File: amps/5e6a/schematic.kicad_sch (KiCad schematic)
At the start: 62 parts, among them T3 part not legible

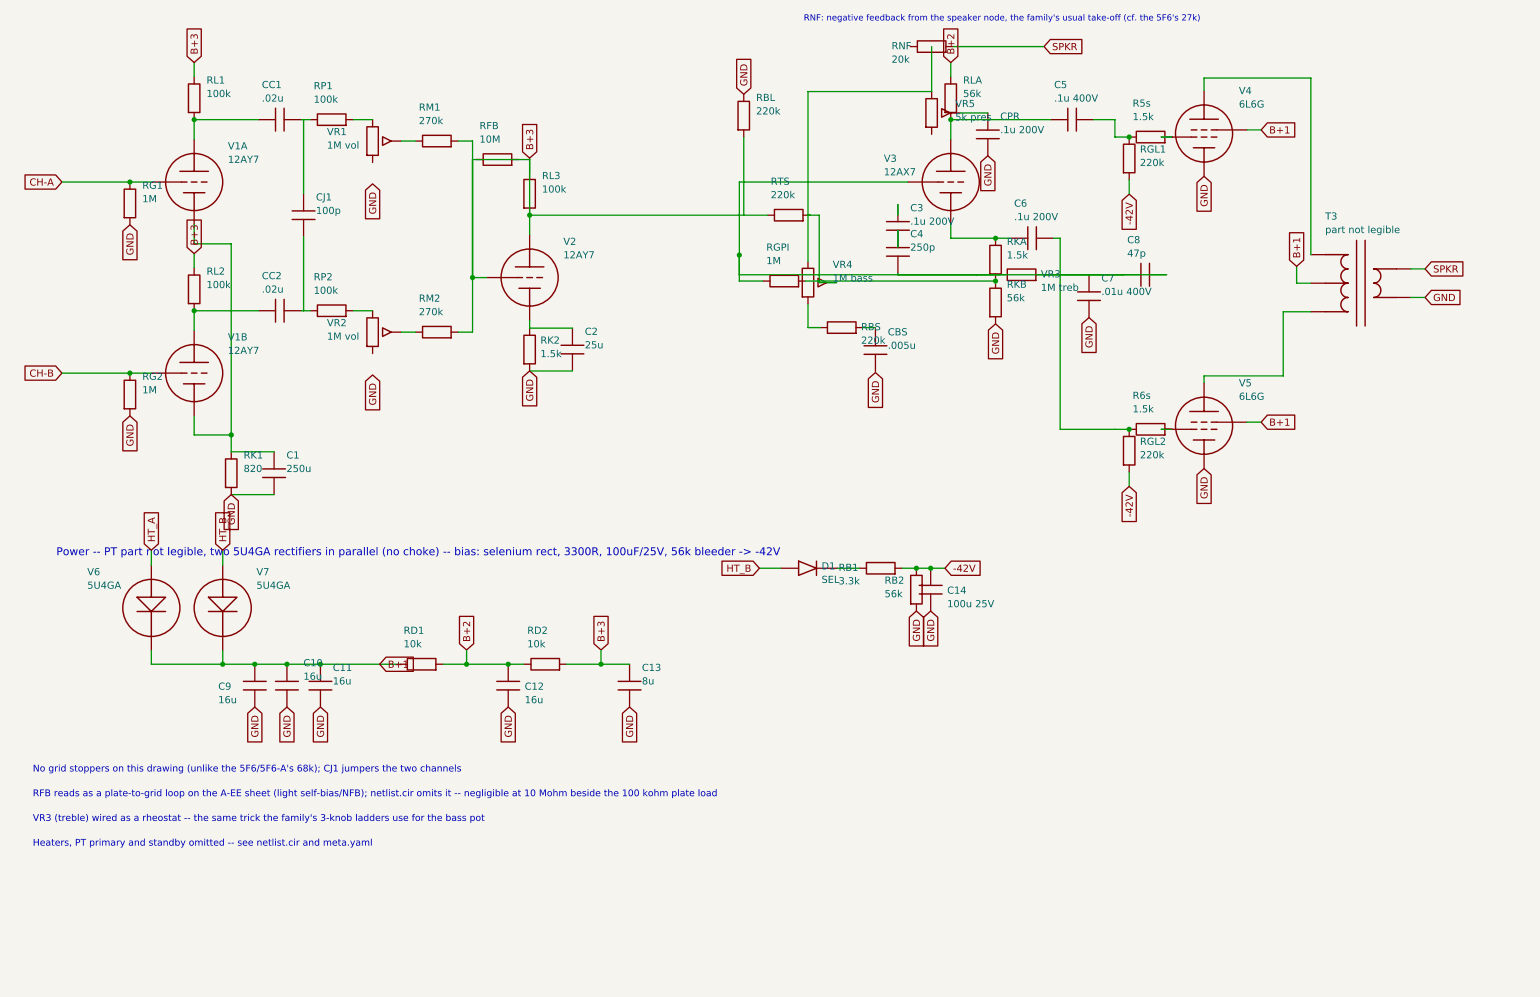
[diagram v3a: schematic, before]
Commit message: Fix: deterministic schematic ids and wires split at every join
- _u() is uuid5 over (amp id, emission order), so a regeneration of an
  unchanged script is byte-identical and a drift gate becomes possible
- write() splits wire segments at symbol pins, wire ends and junction dots,
  so the file connects exactly what the drawing shows under KiCad's
  endpoint-only semantics (270 pins were on a wire's interior; net
  partitions unchanged on all 38 sheets)
- all sheets regenerated; aa864-bassman title block was stale (draft) and
  now matches meta.yaml (verified)

Co-Authored-By: Claude Fable 5.1 <noreply@anthropic.com>
Claude-Session: https://claude.ai/code/session_01KBMfdh37HmCL2iWcBiL5J1
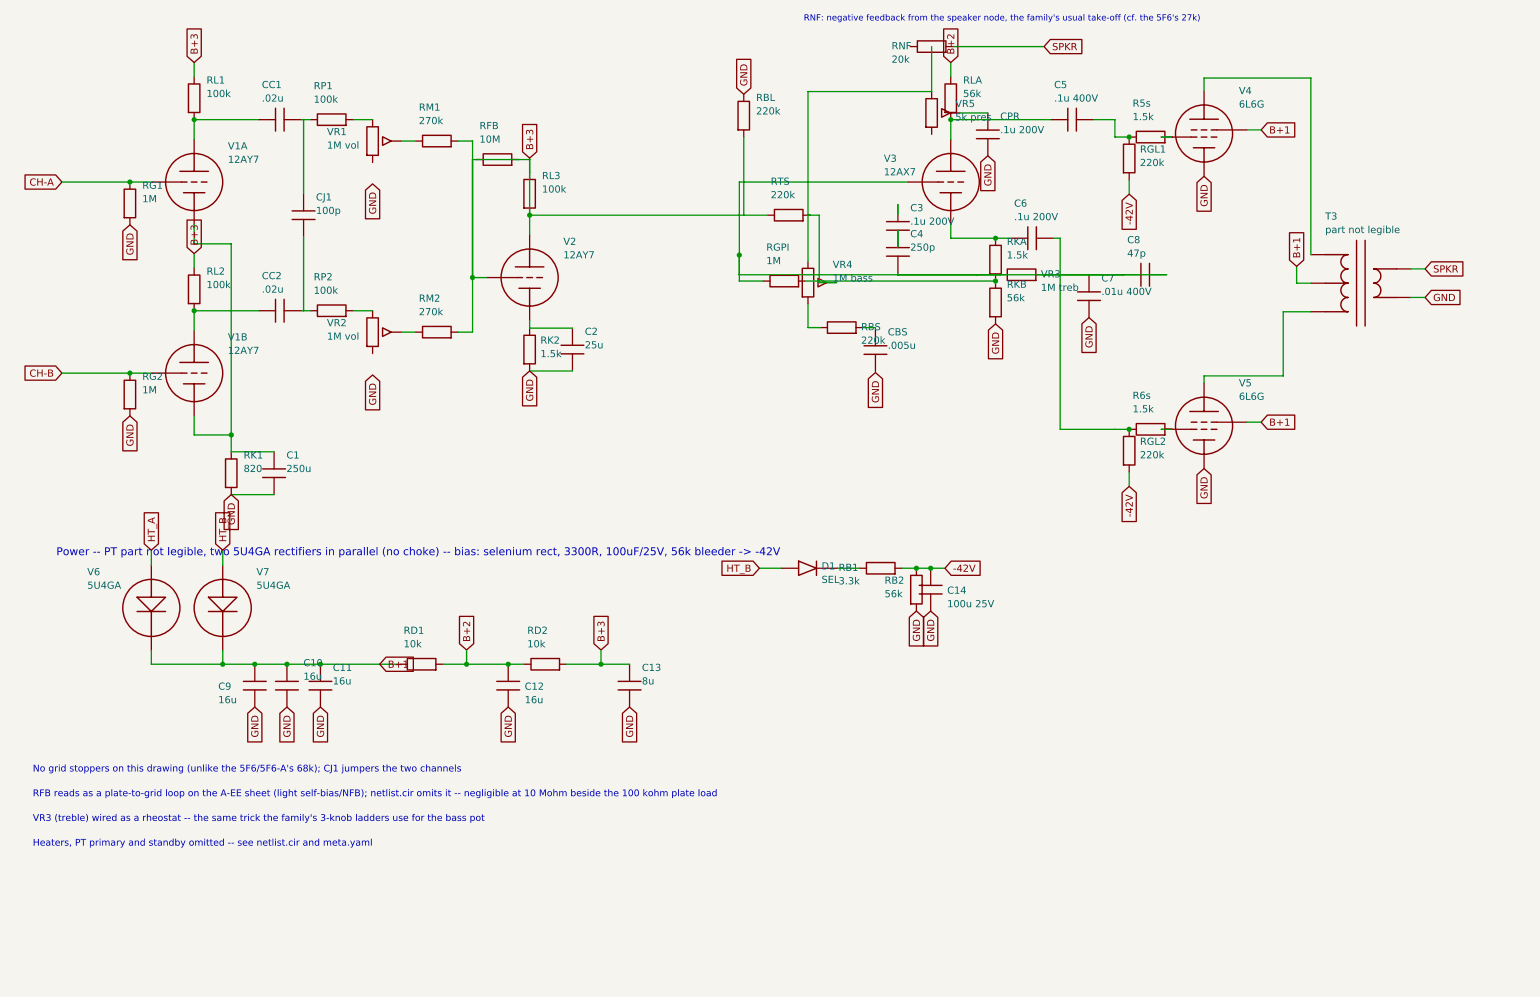
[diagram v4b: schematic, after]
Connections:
- net B+3: now also RFB.1, RFB.2
- net at RTS.2, VR4.2 (W): now also VR4.1, VR5.1
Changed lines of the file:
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@@
     (property "Reference" "V1A" (at 47.4116 36.07 0) (effects (font (size 1.27 1.27)) (justify left)))
     (property "Value" "12AY7" (at 47.4116 38.47 0) (effects (font (size 1.27 1.27)) (justify left))))
-  (wire (pts (xy 17.8816 42.47) (xy 33.7916 42.47))
+  (wire (pts (xy 17.8816 42.47) (xy 29.9816 42.47))
+    (stroke (width 0) (type default)))
+  (wire (pts (xy 29.9816 42.47) (xy 33.7916 42.47))
     (stroke (width 0) (type default)))
   (junction (at 29.9816 42.47) (diameter 0) (color 0 0 0 0))
@@
   (wire (pts (xy 88.4016 35.18) (xy 90.9416 35.18))
     (stroke (width 0) (type default)))
-  (wire (pts (xy 90.9416 35.18) (xy 90.9416 59.47))
+  (wire (pts (xy 90.9416 35.18) (xy 90.9416 38.47))
+    (stroke (width 0) (type default)))
+  (wire (pts (xy 90.9416 38.47) (xy 90.9416 59.47))
     (stroke (width 0) (type default)))
   (global_label "CH-B" (shape input) (at 17.8816 76.47 180)
@@
     (property "Reference" "V1B" (at 47.4116 70.07 0) (effects (font (size 1.27 1.27)) (justify left)))
     (property "Value" "12AY7" (at 47.4116 72.47 0) (effects (font (size 1.27 1.27)) (justify left))))
-  (wire (pts (xy 17.8816 76.47) (xy 33.7916 76.47))
+  (wire (pts (xy 17.8816 76.47) (xy 29.9816 76.47))
+    (stroke (width 0) (type default)))
+  (wire (pts (xy 29.9816 76.47) (xy 33.7916 76.47))
     (stroke (width 0) (type default)))
   (junction (at 29.9816 76.47) (diameter 0) (color 0 0 0 0))
@@
   (wire (pts (xy 41.4116 87.47) (xy 48.0116 87.47))
     (stroke (width 0) (type default)))
-  (wire (pts (xy 48.0116 53.47) (xy 48.0116 90.47))
+  (wire (pts (xy 48.0116 53.47) (xy 48.0116 87.47))
+    (stroke (width 0) (type default)))
+  (wire (pts (xy 48.0116 87.47) (xy 48.0116 90.47))
     (stroke (width 0) (type default)))
   (junction (at 48.0116 87.47) (diameter 0) (color 0 0 0 0))
@@
     (property "Reference" "RL3" (at 103.302 41.36 0) (effects (font (size 1.27 1.27)) (justify left)))
     (property "Value" "100k" (at 103.302 43.76 0) (effects (font (size 1.27 1.27)) (justify left))))
-  (wire (pts (xy 101.102 40.75) (xy 101.102 38.21))
+  (wire (pts (xy 101.102 40.75) (xy 101.102 38.47))
+    (stroke (width 0) (type default)))
+  (wire (pts (xy 101.102 38.47) (xy 101.102 38.21))
     (stroke (width 0) (type default)))
   (global_label "B+3" (shape input) (at 101.102 38.21 90)
     (effects (font (size 1.27 1.27)) (justify left)))
-  (wire (pts (xy 101.102 48.37) (xy 101.102 38.47))
-    (stroke (width 0) (type default)))
-  (wire (pts (xy 101.102 38.47) (xy 90.9416 38.47))
+  (wire (pts (xy 101.102 48.37) (xy 101.102 40.75))
+    (stroke (width 0) (type default)))
+  (wire (pts (xy 101.102 40.75) (xy 101.102 38.47))
+    (stroke (width 0) (type default)))
+  (wire (pts (xy 101.102 38.47) (xy 99.1916 38.47))
+    (stroke (width 0) (type default)))
+  (wire (pts (xy 99.1916 38.47) (xy 91.5716 38.47))
+    (stroke (width 0) (type default)))
+  (wire (pts (xy 91.5716 38.47) (xy 90.9416 38.47))
     (stroke (width 0) (type default)))
   (wire (pts (xy 90.9416 38.47) (xy 90.9416 59.47))
@@
     (property "Reference" "VR4" (at 155.032 57.17 0) (effects (font (size 1.27 1.27)) (justify left)))
     (property "Value" "1M bass" (at 155.032 59.57 0) (effects (font (size 1.27 1.27)) (justify left))))
-  (wire (pts (xy 150.632 48.37) (xy 152.632 48.37))
+  (wire (pts (xy 150.632 48.37) (xy 151.012 48.37))
+    (stroke (width 0) (type default)))
+  (wire (pts (xy 151.012 48.37) (xy 152.632 48.37))
     (stroke (width 0) (type default)))
   (wire (pts (xy 152.632 48.37) (xy 152.632 60.37))
@@
   (wire (pts (xy 152.632 60.37) (xy 155.712 60.37))
     (stroke (width 0) (type default)))
-  (wire (pts (xy 150.632 56.56) (xy 150.632 26.37))
+  (wire (pts (xy 150.632 56.56) (xy 150.632 48.37))
+    (stroke (width 0) (type default)))
+  (wire (pts (xy 150.632 48.37) (xy 150.632 26.37))
     (stroke (width 0) (type default)))
   (symbol (lib_id "cx:R") (at 156.632 68.37 90) (unit 1)
@@
     (property "Reference" "V3" (at 164.127 38.29 0) (effects (font (size 1.27 1.27)) (justify left)))
     (property "Value" "12AX7" (at 164.127 40.69 0) (effects (font (size 1.27 1.27)) (justify left))))
-  (wire (pts (xy 214.442 58.97) (xy 138.412 58.97))
-    (stroke (width 0) (type default)))
-  (wire (pts (xy 138.412 58.97) (xy 138.412 42.47))
+  (wire (pts (xy 214.442 58.97) (xy 206.822 58.97))
+    (stroke (width 0) (type default)))
+  (wire (pts (xy 206.822 58.97) (xy 200.632 58.97))
+    (stroke (width 0) (type default)))
+  (wire (pts (xy 200.632 58.97) (xy 192.442 58.97))
+    (stroke (width 0) (type default)))
+  (wire (pts (xy 192.442 58.97) (xy 184.822 58.97))
+    (stroke (width 0) (type default)))
+  (wire (pts (xy 184.822 58.97) (xy 180.632 58.97))
+    (stroke (width 0) (type default)))
+  (wire (pts (xy 180.632 58.97) (xy 166.632 58.97))
+    (stroke (width 0) (type default)))
+  (wire (pts (xy 166.632 58.97) (xy 138.412 58.97))
+    (stroke (width 0) (type default)))
+  (wire (pts (xy 138.412 58.97) (xy 138.412 55.47))
+    (stroke (width 0) (type default)))
+  (wire (pts (xy 138.412 55.47) (xy 138.412 42.47))
     (stroke (width 0) (type default)))
   (wire (pts (xy 138.412 42.47) (xy 168.412 42.47))
@@
   (global_label "GND" (shape input) (at 184.002 67.71 270)
     (effects (font (size 1.27 1.27)) (justify right)))
-  (wire (pts (xy 138.412 55.47) (xy 138.412 60.09))
+  (wire (pts (xy 138.412 55.47) (xy 138.412 58.97))
+    (stroke (width 0) (type default)))
+  (wire (pts (xy 138.412 58.97) (xy 138.412 60.09))
     (stroke (width 0) (type default)))
   (junction (at 138.412 55.47) (diameter 0) (color 0 0 0 0))
@@
   (wire (pts (xy 46.4916 125.87) (xy 46.4916 128.27))
     (stroke (width 0) (type default)))
-  (wire (pts (xy 33.7916 128.27) (xy 74.4316 128.27))
+  (wire (pts (xy 33.7916 128.27) (xy 46.4916 128.27))
+    (stroke (width 0) (type default)))
+  (wire (pts (xy 46.4916 128.27) (xy 52.2016 128.27))
+    (stroke (width 0) (type default)))
+  (wire (pts (xy 52.2016 128.27) (xy 57.9216 128.27))
+    (stroke (width 0) (type default)))
+  (wire (pts (xy 57.9216 128.27) (xy 63.8816 128.27))
+    (stroke (width 0) (type default)))
+  (wire (pts (xy 63.8816 128.27) (xy 74.4316 128.27))
     (stroke (width 0) (type default)))
   (junction (at 46.4916 128.27) (diameter 0) (color 0 0 0 0))
@@
   (wire (pts (xy 74.4316 128.27) (xy 78.0716 128.27))
     (stroke (width 0) (type default)))
-  (wire (pts (xy 85.6916 128.27) (xy 97.2916 128.27))
+  (wire (pts (xy 85.6916 128.27) (xy 89.8816 128.27))
+    (stroke (width 0) (type default)))
+  (wire (pts (xy 89.8816 128.27) (xy 97.2916 128.27))
     (stroke (width 0) (type default)))
   (junction (at 89.8816 128.27) (diameter 0) (color 0 0 0 0))
@@
   (wire (pts (xy 97.2916 128.27) (xy 100.072 128.27))
     (stroke (width 0) (type default)))
-  (wire (pts (xy 107.692 128.27) (xy 118.882 128.27))
+  (wire (pts (xy 107.692 128.27) (xy 113.802 128.27))
+    (stroke (width 0) (type default)))
+  (wire (pts (xy 113.802 128.27) (xy 118.882 128.27))
     (stroke (width 0) (type default)))
   (junction (at 113.802 128.27) (diameter 0) (color 0 0 0 0))
@@
   (wire (pts (xy 159.762 111.19) (xy 159.762 111.19))
     (stroke (width 0) (type default)))
-  (wire (pts (xy 167.382 111.19) (xy 175.002 111.19))
+  (wire (pts (xy 167.382 111.19) (xy 169.922 111.19))
+    (stroke (width 0) (type default)))
+  (wire (pts (xy 169.922 111.19) (xy 172.462 111.19))
+    (stroke (width 0) (type default)))
+  (wire (pts (xy 172.462 111.19) (xy 175.002 111.19))
     (stroke (width 0) (type default)))
   (junction (at 169.922 111.19) (diameter 0) (color 0 0 0 0))
